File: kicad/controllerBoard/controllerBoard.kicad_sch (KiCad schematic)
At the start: 4 parts, among them J1 Conn_02x20_Top_Bottom, J2 Conn_02x20_Top_Bottom

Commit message: update main board schematic
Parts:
- C1: footprint (none) -> Capacitor_SMD:C_1206_3216Metric
- C2: footprint (none) -> Capacitor_SMD:C_0805_2012Metric
- J1, J2: footprint Connector:CUI_PD-30 -> Connector_IDC:IDC-Header_2x20_P2.54mm_Horizontal
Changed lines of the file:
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@@
 			)
 		)
-		(property "Footprint" ""
+		(property "Footprint" "Capacitor_SMD:C_0805_2012Metric"
 			(at 40.3352 161.29 0)
 			(hide yes)
@@
 			)
 		)
-		(property "Footprint" ""
+		(property "Footprint" "Capacitor_SMD:C_1206_3216Metric"
 			(at 22.5552 161.29 0)
 			(hide yes)
@@
 			)
 		)
-		(property "Footprint" "Connector:CUI_PD-30"
+		(property "Footprint" "Connector_IDC:IDC-Header_2x20_P2.54mm_Horizontal"
 			(at 73.66 46.99 0)
 			(hide yes)
@@
 			)
 		)
-		(property "Footprint" "Connector:CUI_PD-30"
+		(property "Footprint" "Connector_IDC:IDC-Header_2x20_P2.54mm_Horizontal"
 			(at 36.83 46.99 0)
 			(hide yes)

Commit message: finished routing all sub schematics
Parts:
- removed C1: 47uC, Capacitor_SMD:C_1206_3216Metric, symbol Device:C
- removed C2: 100nC, Capacitor_SMD:C_0805_2012Metric, symbol Device:C
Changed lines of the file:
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@@
-	)
-	(symbol
-		(lib_id "Device:C")
-		(at 39.37 157.48 0)
-		(unit 1)
-		(body_style 1)
-		(exclude_from_sim no)
-		(in_bom yes)
-		(on_board yes)
-		(in_pos_files yes)
-		(dnp no)
-		(fields_autoplaced yes)
-		(property "Reference" "C2"
-			(at 43.18 156.2099 0)
-			(show_name no)
-			(do_not_autoplace no)
-			(effects
-				(font
-					(size 1.27 1.27)
-				)
-				(justify left)
-			)
-		)
-		(property "Value" "100nC"
-			(at 43.18 158.7499 0)
-			(show_name no)
-			(do_not_autoplace no)
-			(effects
-				(font
-					(size 1.27 1.27)
-				)
-				(justify left)
-			)
-		)
-		(property "Footprint" "Capacitor_SMD:C_0805_2012Metric"
-			(at 40.3352 161.29 0)
-			(hide yes)
-			(show_name no)
-			(do_not_autoplace no)
-			(effects
-				(font
-					(size 1.27 1.27)
-				)
-			)
-		)
-		(property "Datasheet" ""
-			(at 39.37 157.48 0)
-			(hide yes)
-			(show_name no)
-			(do_not_autoplace no)
-			(effects
-				(font
-					(size 1.27 1.27)
-				)
-			)
-		)
-		(property "Description" "Unpolarized capacitor"
-			(at 39.37 157.48 0)
-			(hide yes)
-			(show_name no)
-			(do_not_autoplace no)
-			(effects
-				(font
-					(size 1.27 1.27)
-				)
-			)
-		)
-		(pin "1"
-		)
-		(pin "2"
-		)
-		(instances
-			(project "controllerBoard"
-				(path "/93a9a1ca-4ee5-40da-ab67-92836146c003"
-					(reference "C2")
-					(unit 1)
-				)
-			)
-		)
 	)
 	(symbol
@@
 					(unit 1)
 				)
-			)
-		)
-	)
-	(symbol
-		(lib_id "Device:C")
-		(at 21.59 157.48 0)
-		(unit 1)
-		(body_style 1)
-		(exclude_from_sim no)
-		(in_bom yes)
-		(on_board yes)
-		(in_pos_files yes)
-		(dnp no)
-		(fields_autoplaced yes)
-		(property "Reference" "C1"
-			(at 25.4 156.2099 0)
-			(show_name no)
-			(do_not_autoplace no)
-			(effects
-				(font
-					(size 1.27 1.27)
-				)
-				(justify left)
-			)
-		)
-		(property "Value" "47uC"
-			(at 25.4 158.7499 0)
-			(show_name no)
-			(do_not_autoplace no)
-			(effects
-				(font
-					(size 1.27 1.27)
-				)
-				(justify left)
-			)
-		)
-		(property "Footprint" "Capacitor_SMD:C_1206_3216Metric"
-			(at 22.5552 161.29 0)
-			(hide yes)
-			(show_name no)
-			(do_not_autoplace no)
-			(effects
-				(font
-					(size 1.27 1.27)
-				)
-			)
-		)
-		(property "Datasheet" ""
-			(at 21.59 157.48 0)
-			(hide yes)
-			(show_name no)
-			(do_not_autoplace no)
-			(effects
-				(font
-					(size 1.27 1.27)
-				)
-			)
-		)
-		(property "Description" "Unpolarized capacitor"
-			(at 21.59 157.48 0)
-			(hide yes)
-			(show_name no)
-			(do_not_autoplace no)
-			(effects
-				(font
-					(size 1.27 1.27)
-				)
-			)
-		)
-		(pin "1"
-		)
-		(pin "2"
-		)
-		(instances
-			(project "controllerBoard"
-				(path "/93a9a1ca-4ee5-40da-ab67-92836146c003"
-					(reference "C1")
-					(unit 1)
-				)

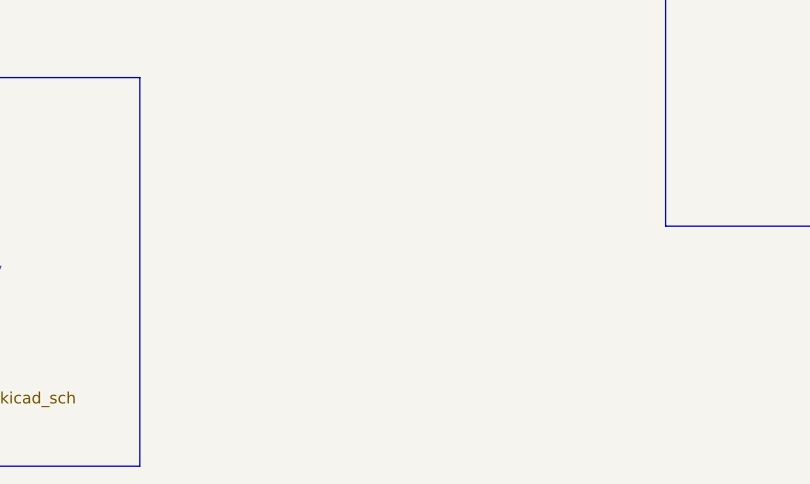
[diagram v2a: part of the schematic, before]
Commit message: add mounting holes
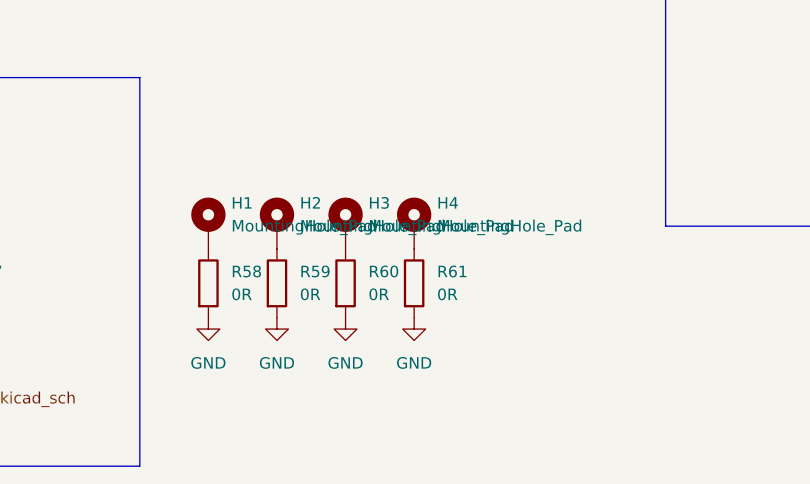
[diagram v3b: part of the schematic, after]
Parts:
- added H1, H2, H3, H4: MountingHole_Pad, MountingHole:MountingHole_3.2mm_M3_DIN965_Pad, symbol Mechanical:MountingHole_Pad
- added R58, R59, R60, R61: 0R, Resistor_SMD:R_1206_3216Metric_Pad1.30x1.75mm_HandSolder, symbol Device:R
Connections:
- net GND: now also R58.2, R59.2, R60.2, R61.2
- new net: H2.1, R59.1
- new net: H1.1, R58.1
- new net: H3.1, R60.1
- new net: H4.1, R61.1

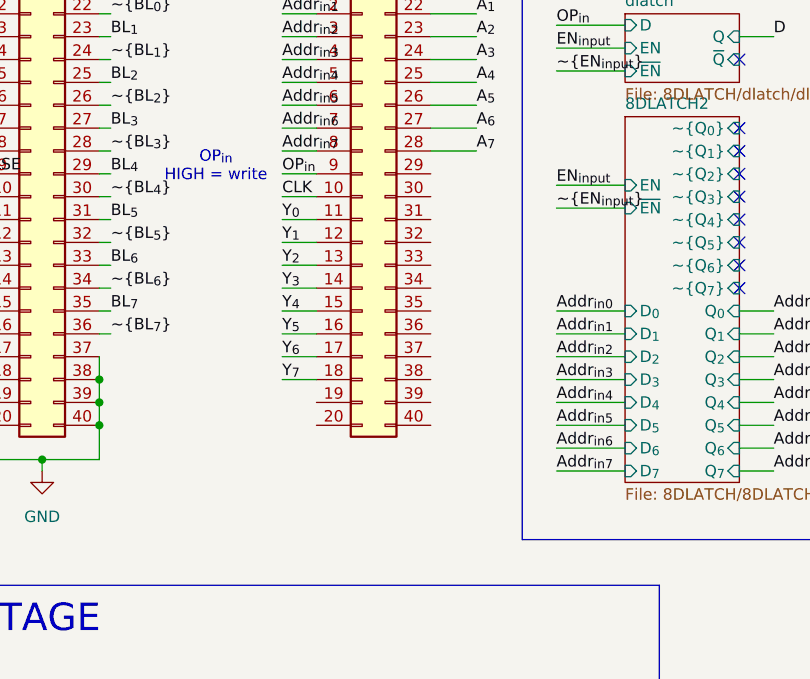
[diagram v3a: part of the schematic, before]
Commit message: Add breakout board through holes on main ram board
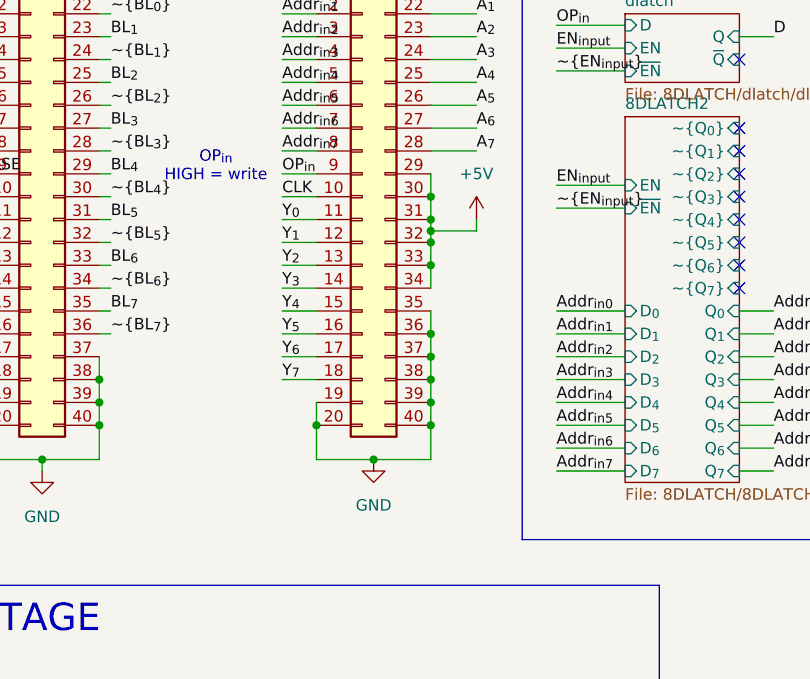
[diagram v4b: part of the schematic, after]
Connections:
- net +5V: now also J2.29 (Pin_29), J2.30 (Pin_30), J2.31 (Pin_31), J2.32 (Pin_32), J2.33 (Pin_33), J2.34 (Pin_34)
- net GND: now also J2.19 (Pin_19), J2.20 (Pin_20), J2.35 (Pin_35), J2.36 (Pin_36), J2.37 (Pin_37), J2.38 (Pin_38), J2.39 (Pin_39), J2.40 (Pin_40)

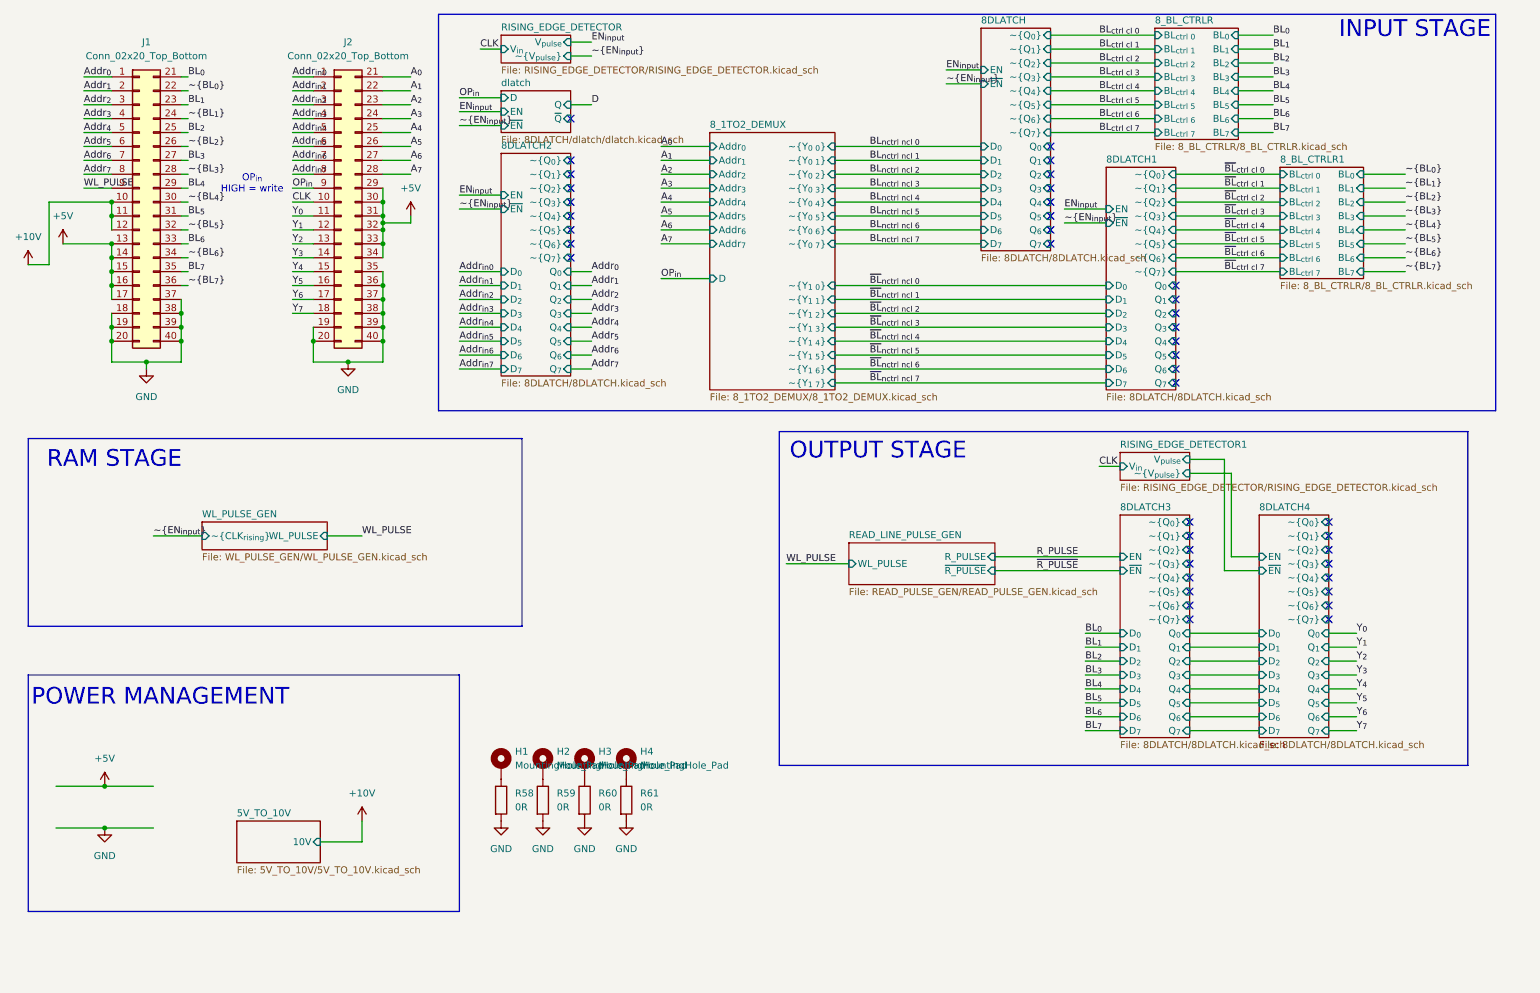
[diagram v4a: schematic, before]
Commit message: update bom, add more capacitors
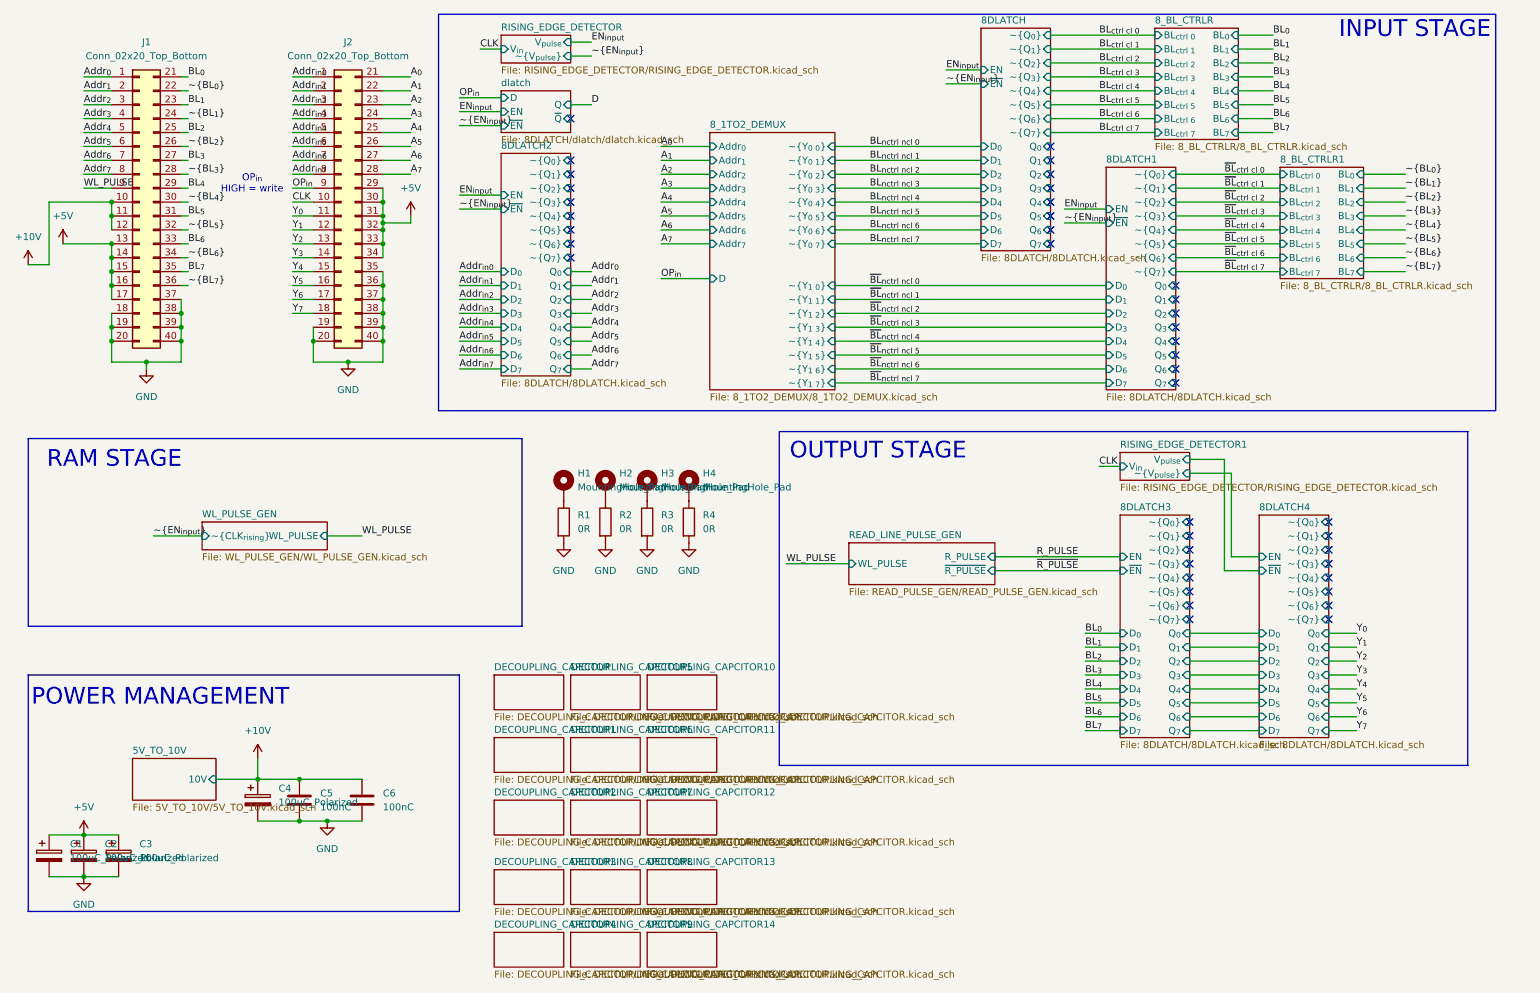
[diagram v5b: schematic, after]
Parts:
- added C1, C2, C3, C4: 100uC_Polarized, Capacitor_SMD:CP_Elec_6.3x7.7, symbol Device:C_Polarized
- added C5, C6: 100nC, Capacitor_SMD:C_0805_2012Metric_Pad1.18x1.45mm_HandSolder, symbol Device:C
- renumbered R58 to R1, R59 to R2, R60 to R3, R61 to R4
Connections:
- net +10V: now also C4.1, C5.1, C6.1
- net +5V: now also C1.1, C2.1, C3.1
- net GND: now also C1.2, C2.2, C3.2, C4.2, C5.2, C6.2
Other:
- added sheet DECOUPLING_CAPCITOR (DECOUPLING_CAPCITOR/DECOUPLING_CAPCITOR.kicad_sch)
- added sheet DECOUPLING_CAPCITOR1 (DECOUPLING_CAPCITOR/DECOUPLING_CAPCITOR.kicad_sch)
- added sheet DECOUPLING_CAPCITOR10 (DECOUPLING_CAPCITOR/DECOUPLING_CAPCITOR.kicad_sch)
- added sheet DECOUPLING_CAPCITOR11 (DECOUPLING_CAPCITOR/DECOUPLING_CAPCITOR.kicad_sch)
- added sheet DECOUPLING_CAPCITOR12 (DECOUPLING_CAPCITOR/DECOUPLING_CAPCITOR.kicad_sch)
- added sheet DECOUPLING_CAPCITOR13 (DECOUPLING_CAPCITOR/DECOUPLING_CAPCITOR.kicad_sch)
- added sheet DECOUPLING_CAPCITOR14 (DECOUPLING_CAPCITOR/DECOUPLING_CAPCITOR.kicad_sch)
- added sheet DECOUPLING_CAPCITOR2 (DECOUPLING_CAPCITOR/DECOUPLING_CAPCITOR.kicad_sch)
- added sheet DECOUPLING_CAPCITOR3 (DECOUPLING_CAPCITOR/DECOUPLING_CAPCITOR.kicad_sch)
- added sheet DECOUPLING_CAPCITOR4 (DECOUPLING_CAPCITOR/DECOUPLING_CAPCITOR.kicad_sch)
- added sheet DECOUPLING_CAPCITOR5 (DECOUPLING_CAPCITOR/DECOUPLING_CAPCITOR.kicad_sch)
- added sheet DECOUPLING_CAPCITOR6 (DECOUPLING_CAPCITOR/DECOUPLING_CAPCITOR.kicad_sch)
- added sheet DECOUPLING_CAPCITOR7 (DECOUPLING_CAPCITOR/DECOUPLING_CAPCITOR.kicad_sch)
- added sheet DECOUPLING_CAPCITOR8 (DECOUPLING_CAPCITOR/DECOUPLING_CAPCITOR.kicad_sch)
- added sheet DECOUPLING_CAPCITOR9 (DECOUPLING_CAPCITOR/DECOUPLING_CAPCITOR.kicad_sch)
- moved on the sheet: H1, H2, H3, H4, R1, R2, R3, R4
